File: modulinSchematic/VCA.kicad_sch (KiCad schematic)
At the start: 0 parts

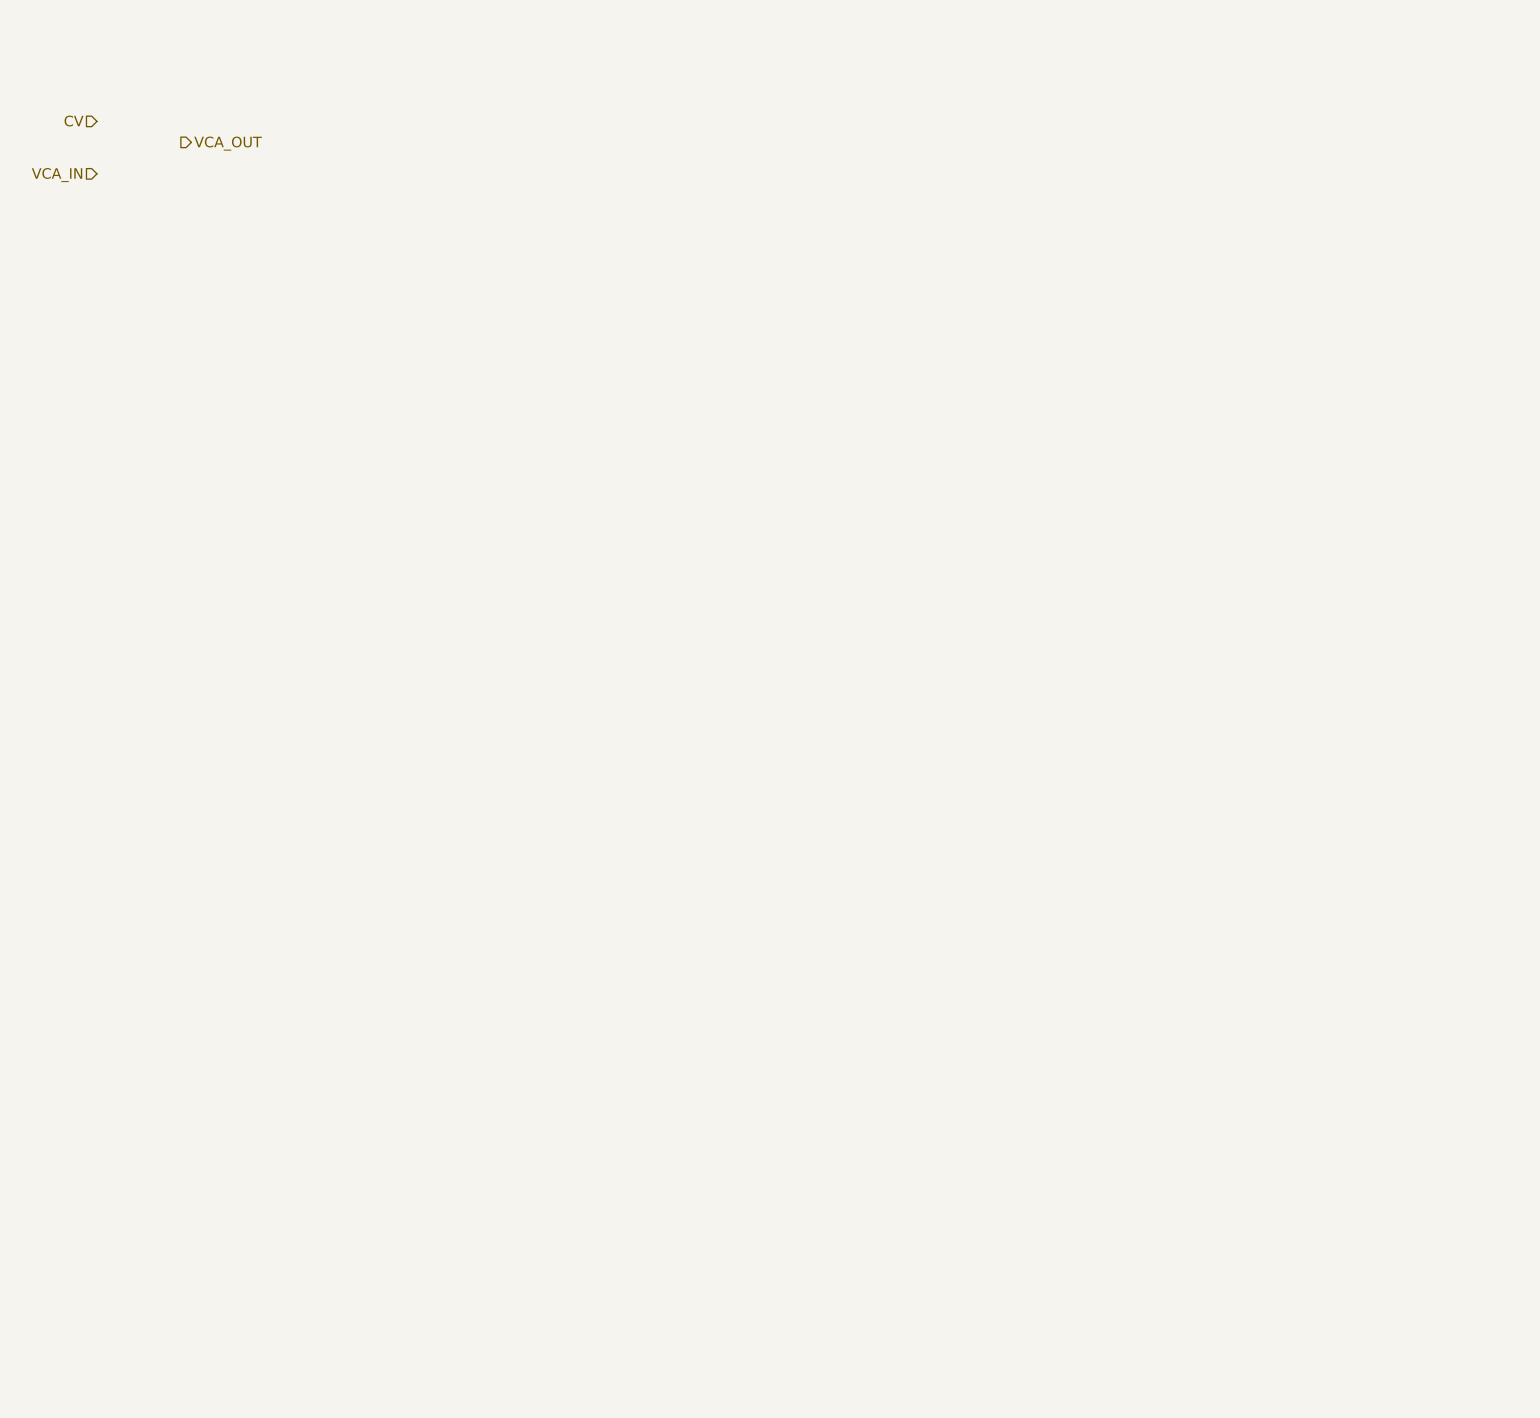
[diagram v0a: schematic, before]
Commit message: Add power schematic
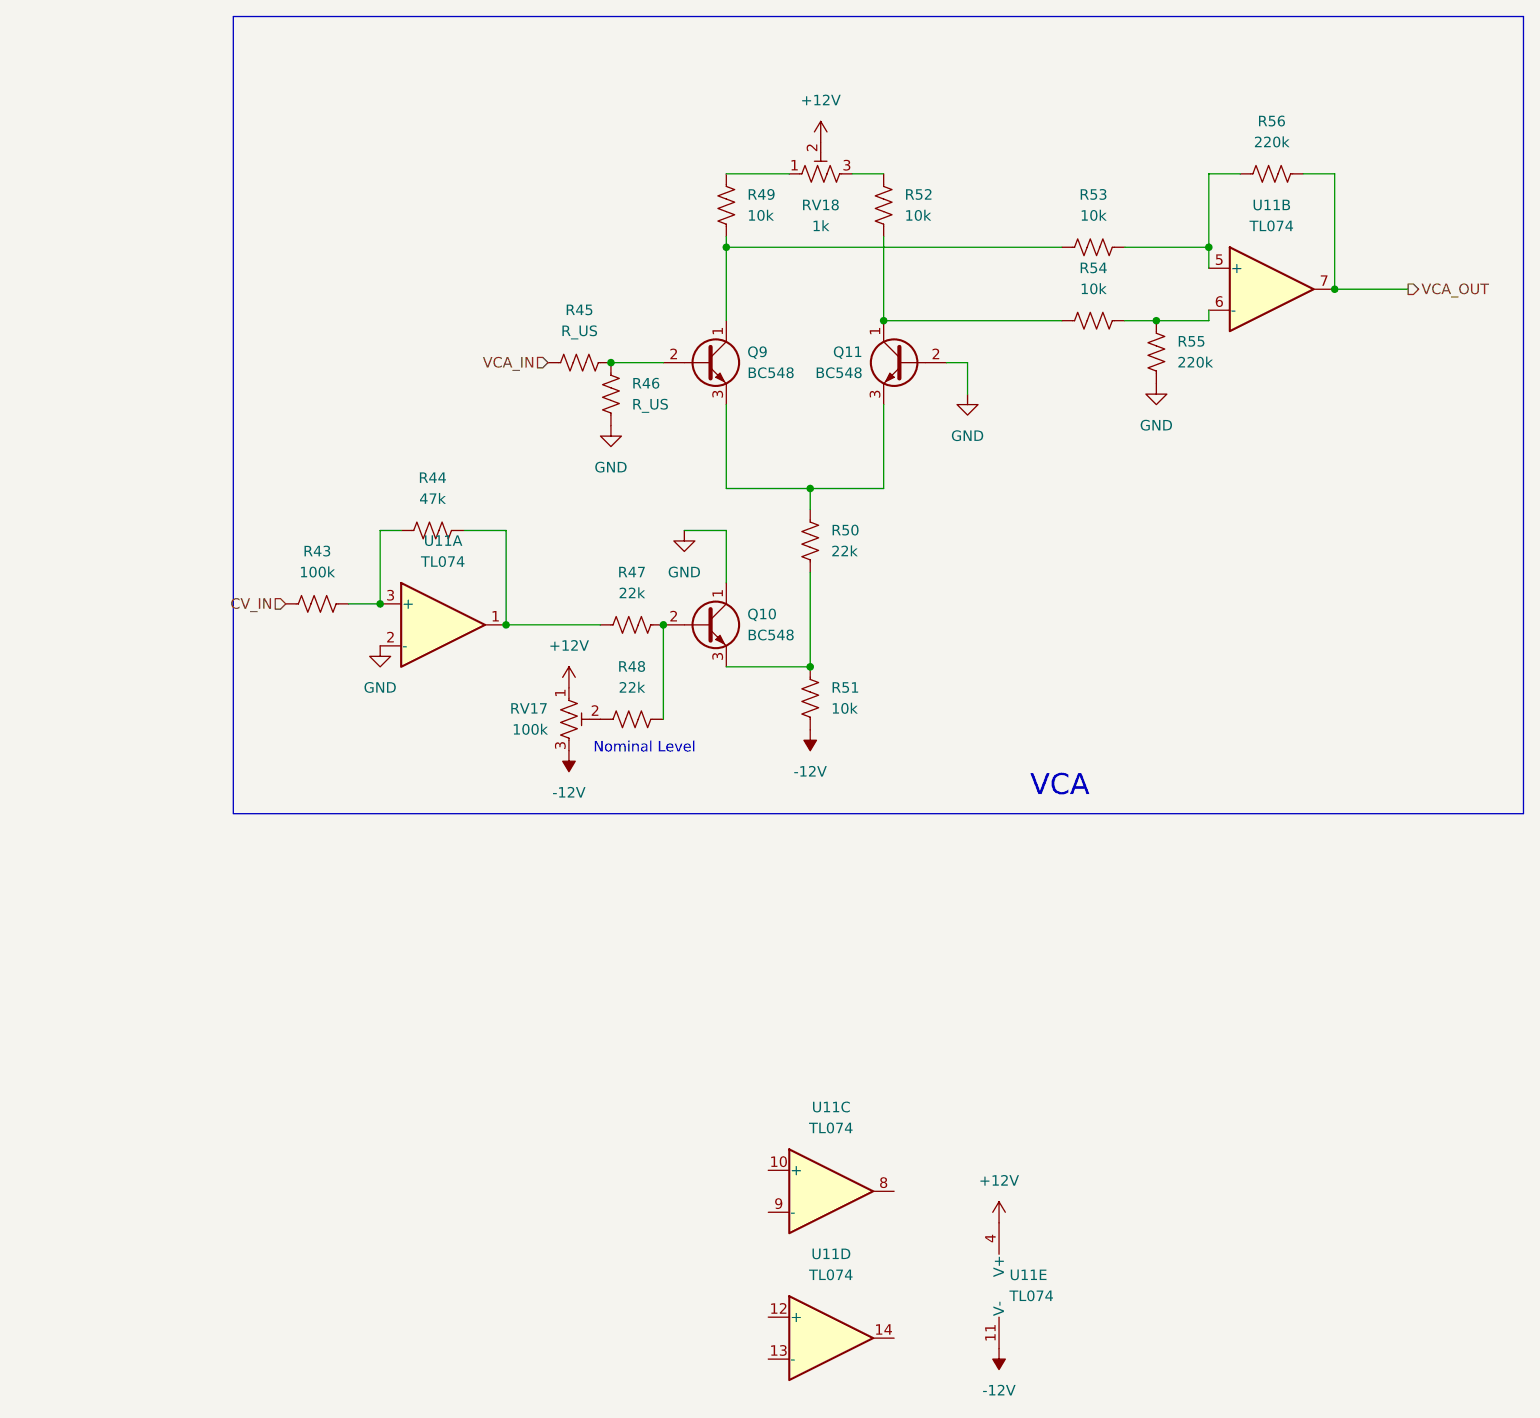
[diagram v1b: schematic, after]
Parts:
- added Q10, Q11, Q9: BC548, Package_TO_SOT_THT:TO-92_Inline, symbol Transistor_BJT:BC548
- added R43: 100k, Resistor_THT:R_Axial_DIN0207_L6.3mm_D2.5mm_P10.16mm_Horizontal, symbol Device:R_US
- added R44: 47k, Resistor_THT:R_Axial_DIN0207_L6.3mm_D2.5mm_P10.16mm_Horizontal, symbol Device:R_US
- added R45, R46: R_US, Resistor_THT:R_Axial_DIN0207_L6.3mm_D2.5mm_P10.16mm_Horizontal, symbol Device:R_US
- added R47, R48, R50: 22k, Resistor_THT:R_Axial_DIN0207_L6.3mm_D2.5mm_P10.16mm_Horizontal, symbol Device:R_US
- added R49, R51, R52, R53, R54: 10k, Resistor_THT:R_Axial_DIN0207_L6.3mm_D2.5mm_P10.16mm_Horizontal, symbol Device:R_US
- added R55, R56: 220k, Resistor_THT:R_Axial_DIN0207_L6.3mm_D2.5mm_P10.16mm_Horizontal, symbol Device:R_US
- added RV17: 100k, Potentiometer_THT:Potentiometer_Bourns_3266Y_Vertical, symbol Device:R_Potentiometer_Trim_US
- added RV18: 1k, Potentiometer_THT:Potentiometer_Bourns_3266Y_Vertical, symbol Device:R_Potentiometer_Trim_US
- added U11: TL074, symbol Amplifier_Operational:TL074
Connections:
- net VCA_IN: now also R45.1
- net VCA_OUT: now also R56.2, U11.7
- new net: Q10.3 (E), R50.1, R51.2
- new net: R54.1, R55.1, U11.6 (-)
- new net: R44.2, R47.1, U11.1
- new net: Q10.2 (B), R47.2, R48.2
- new net: Q11.3 (E), Q9.3 (E), R50.2
- new net: Q9.1 (C), R49.1, R53.2
- new net: Q9.2 (B), R45.2, R46.2
- new net: Q11.1 (C), R52.1, R54.2
- new net: R52.2, RV18.3
- new net: R53.1, R56.1, U11.5 (+)
- new net: R43.2, R44.1, U11.3 (+)
- new net: R49.2, RV18.1
- new net: R48.1, RV17.2
- new net +12V: RV17.1, RV18.2, U11.4 (V+)
- new net -12V: R51.1, RV17.3, U11.11 (V-)
- new net CV_IN: R43.1
- new net GND: Q10.1 (C), Q11.2 (B), R46.1, R55.2, U11.2 (-)
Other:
- note added: "Nominal Level"
- note added: "VCA"
